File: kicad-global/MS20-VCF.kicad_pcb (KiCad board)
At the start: 2 copper layers, 207 x 128.5 mm, 116 parts, among them J1 FilterCV1, J10 Conn_JackBoard, J11 FilterCV2, J12 FilterOut2, J13 Conn_CircuitBoard, J14 Conn_JackBoard, J15 FilterIn2, J2 FilterOut1, J3 Conn_CircuitBoard, J4 Conn_JackBoard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

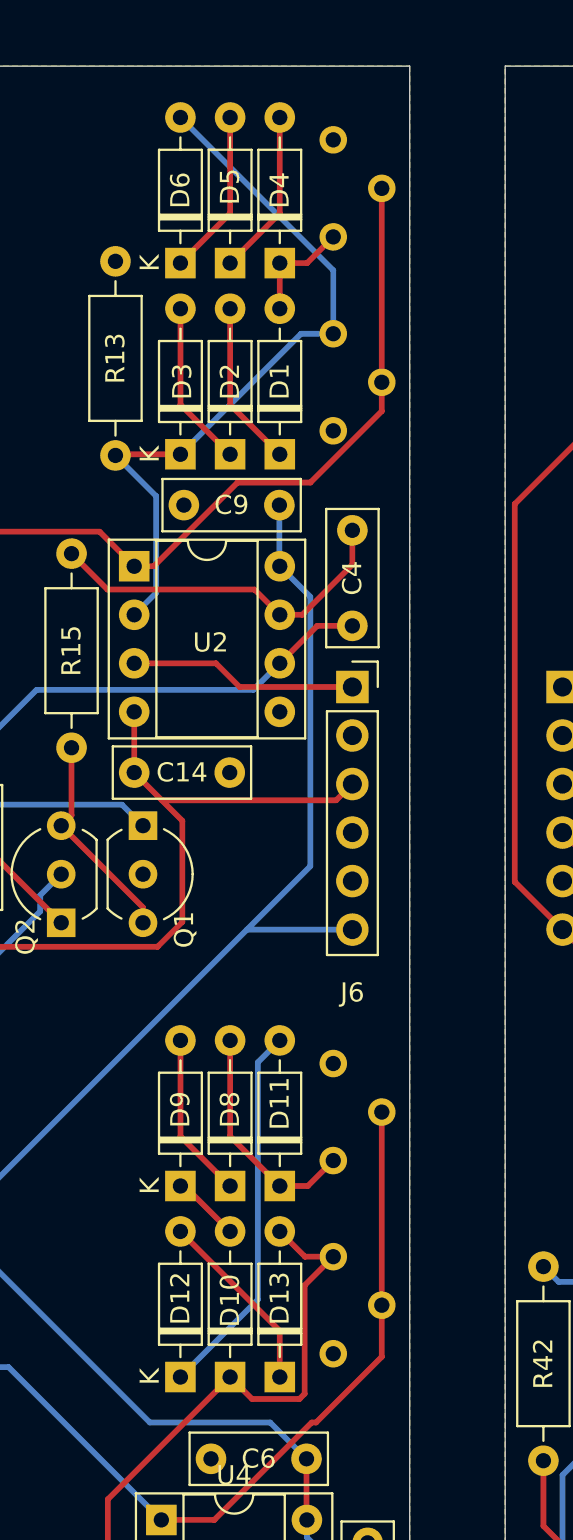
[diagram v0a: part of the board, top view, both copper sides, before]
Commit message: update worflow run condition + trimmer footprint update
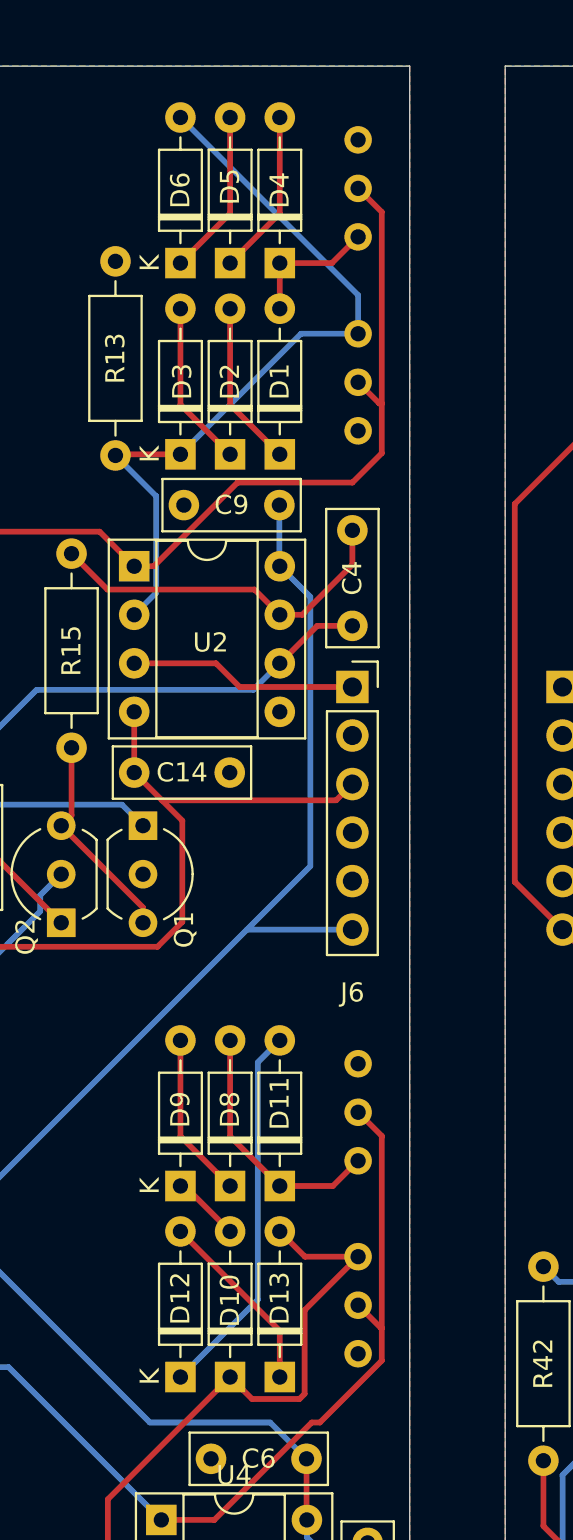
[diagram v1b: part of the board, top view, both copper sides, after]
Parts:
- C1, C15: value 10µF -> 10uF
- C10, C5: value 10µ -> 10uF
- ResLv1: value 5k -> 10k; footprint Potentiometer_THT:Potentiometer_Bourns_3386X_Horizontal -> Potentiometer_THT:Potentiometer_Bourns_3386C_Horizontal
- ResLv2, ResVol1, ResVol2: footprint Potentiometer_THT:Potentiometer_Bourns_3386X_Horizontal -> Potentiometer_THT:Potentiometer_Bourns_3386C_Horizontal
- moved ResVol2 1.30 mm to (87.3, 93.8)
- moved ResLv1 1.30 mm to (87.3, 55.6)
- moved ResLv2 1.30 mm to (87.3, 103.9)
- moved ResVol1 1.30 mm to (87.3, 45.4)
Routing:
- net Net-(C2-Pad2): track 43.5 -> 47.0 mm
- net Net-(C16-Pad2): track 52.8 -> 55.2 mm
- net Net-(D3-Pad1): track 38.4 -> 40.2 mm
- net Net-(D10-Pad1): track 31.1 -> 32.9 mm
- net Net-(D1-Pad2): track 5.76 -> 7.06 mm
- net Net-(D11-Pad1): track 12.0 -> 13.3 mm

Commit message: update front panel and infos on components
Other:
- board text added: "Double MS-20 VCF V1.3 BleepSound 2023"
- board text removed: "Double MS-20 VCF V1.2 BleepSound 2022"

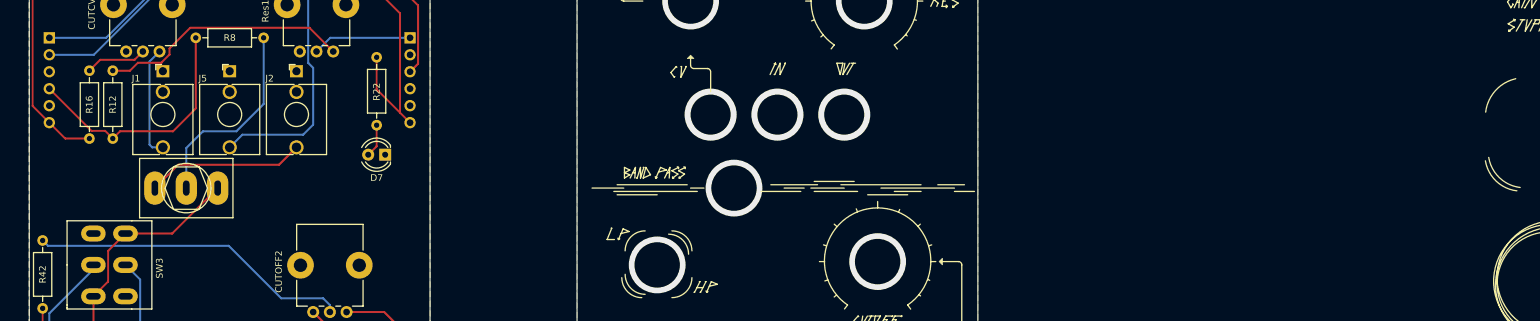
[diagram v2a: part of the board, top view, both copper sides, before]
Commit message: update documentation + update repo layout
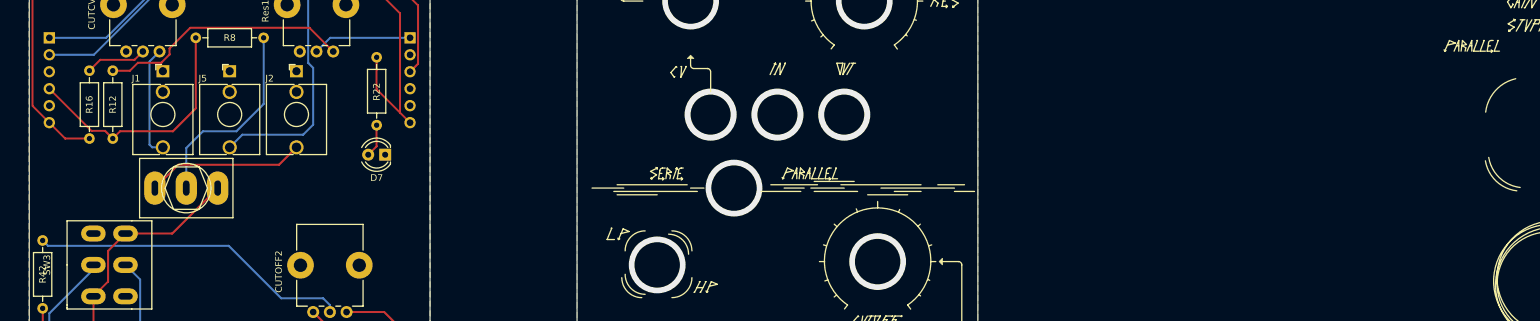
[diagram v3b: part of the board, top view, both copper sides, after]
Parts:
- CUTCV1, CUTCV2, CUTOFF1, CUTOFF2, Res1, Res2: footprint Synth:Pot-bourns-alpha -> Kicad-perso:Pot-bourns-alpha
- J1, J11, J12, J15, J2, J5: footprint Synth:Thonkiconn -> Kicad-perso:Thonkiconn
- ResLv2: value 3.3k -> 10k
- SW1, SW3: footprint Synth:SW_DPDT_Toggle -> Kicad-perso:SW_DPDT_Toggle
- SW2: footprint Synth:SW_Toggle_Blue_wSlots -> Kicad-perso:SW_Toggle_Blue_wSlots

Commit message: update version number + hole size on front panel
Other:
- board text added: "Double MS-20 VCF V1.4 BleepSound 2023"
- board text removed: "Double MS-20 VCF V1.3 BleepSound 2023"

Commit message: V2.0
new front panel layout
new normalisation for CV and in/out for bandpass filter
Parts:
- removed FB1, FB2: 10R, Inductor_THT:L_Axial_L7.0mm_D3.3mm_P10.16mm_Horizontal_Fastron_MICC
- removed R22: 2.2k, Resistor_THT:R_Axial_DIN0207_L6.3mm_D2.5mm_P10.16mm_Horizontal
- removed SW2: Bandpass, Kicad-perso:SW_Toggle_Blue_wSlots
- added D14: 1N5819, Diode_THT:D_DO-41_SOD81_P10.16mm_Horizontal, F.Cu at (57.7, 85.3)
- CUTCV1, CUTCV2, CUTOFF1, CUTOFF2, Res1, Res2: value 100k -> B100k
- D7: value LED-12V -> 1N5819; footprint LED_THT:LED_D4.0mm -> Diode_THT:D_DO-41_SOD81_P10.16mm_Horizontal
- J1: value FilterCV1 -> jack
- J11: value FilterCV2 -> jack
- J12: value FilterOut2 -> jack
- J15: value FilterIn2 -> jack
- J2: value FilterOut1 -> jack
- J5: value FilterIn1 -> jack
- ResLv1, ResLv2, ResVol1, ResVol2: footprint Potentiometer_THT:Potentiometer_Bourns_3386C_Horizontal -> Potentiometer_THT:Potentiometer_Bourns_3296W_Vertical
- moved D7 116.1 mm to (32.5, 95.4), turned to 90 degrees
- moved R34 28.7 mm to (105.0, 144.1), turned to 90 degrees
- moved SW3 28.5 mm to (125.0, 125.1)
- moved SW1 28.1 mm to (125.0, 65.6)
- moved R8 24.9 mm to (115.2, 89.0)
- moved R19 24.6 mm to (142.5, 54.8)
- moved R21 24.6 mm to (152.7, 50.8)
- moved R41 16.3 mm to (136.9, 107.7), turned to 0 degrees
- moved CUTOFF1 15.1 mm to (127.5, 49.8)
- moved CUTOFF2 15.0 mm to (127.5, 110.0)
- moved R43 12.4 mm to (147.1, 111.7), turned to 180 degrees
- moved R42 6.30 mm to (103.1, 111.0), turned to 0 degrees
- moved CUTCV1 6.00 mm to (108.5, 71.0)
- moved CUTCV2 6.00 mm to (146.5, 130.1)
- moved Res1 6.00 mm to (146.5, 71.0)
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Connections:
- CUTCV1 pad 1: /CVIn -> GND
- CUTCV1 pad 3: GND -> CV1In
- CUTCV2 pad 1: /Filtre2/CVIn -> GND
- CUTCV2 pad 3: GND -> CV2In
- D7 pad 1: GND -> +12V
- J1 pad T: /CVIn -> CV1In
- J1 pad TN: unconnected-(J1-PadTN) -> CV2In
- J11 pad T: /Filtre2/CVIn -> CV2In
- J11 pad TN: unconnected-(J11-PadTN) -> CV1In
- J15 pad T: Filter2In -> /Filtre2/FilterIn
- J15 pad TN: unconnected-(J15-PadTN) -> Filter2In
- J2 pad T: /JackOut -> /FilterOut
- J2 pad TN: unconnected-(J2-PadTN) -> Filter2In
- J8 pad 10: Net-(J8-Pin_10) -> Net-(D7-A)
- J8 pad 9: Net-(J8-Pin_10) -> Net-(D7-A)
- R19 pad 1: Net-(CUTOFF1-Pad1) -> Net-(CUTOFF1-Pad3)
- R21 pad 2: Net-(CUTOFF1-Pad3) -> Net-(CUTOFF1-Pad1)
- R41 pad 1: Net-(CUTOFF2-Pad1) -> Net-(CUTOFF2-Pad3)
- R43 pad 2: Net-(CUTOFF2-Pad3) -> Net-(CUTOFF2-Pad1)
- Res1 pad 1: Net-(R12-Pad1) -> GND
- Res1 pad 3: GND -> Net-(R12-Pad1)
- Res2 pad 1: Net-(R34-Pad1) -> GND
- Res2 pad 3: GND -> Net-(R34-Pad1)
- SW3 pad 3: Filter2In -> /Filtre2/FilterIn
- SW3 pad 4: Filter2In -> /Filtre2/FilterIn
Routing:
- net CV2In: track 0.00 -> 94.3 mm
- net CV1In: track 0.00 -> 85.9 mm, vias 0 -> 2
- net Net-(CUTOFF2-Pad2): track 48.1 -> 13.2 mm
- net /FilterIn: track 60.5 -> 27.5 mm
- net /Filtre2/FilterIn: track 0.00 -> 29.6 mm
- net /HPass: track 65.3 -> 38.3 mm
- net /LPass: track 57.1 -> 30.1 mm
- net /JackOut: track 23.7 -> 0.00 mm
- net /Out1: track 45.1 -> 26.1 mm
- net /CVIn: track 16.7 -> 0.00 mm
- net /Filtre2/CVIn: track 16.6 -> 0.00 mm
- net Net-(CUTCV2-Pad2): track 55.4 -> 41.0 mm
- net /Filtre2/Out1: track 39.3 -> 24.9 mm
- net Net-(CUTOFF1-Pad2): track 4.10 -> 17.3 mm
- net Net-(J8-Pin_10): track 11.9 -> 0.00 mm
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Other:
- board text added: "Double MS-20 VCF V2.0 BleepSound 2025"
- board text added: "board 1"
- board text added: "board 2"
- board text removed: "Double MS-20 VCF V1.4 BleepSound 2023"
- board text removed: "board 1/2"
- board text removed: "board 2/2"
